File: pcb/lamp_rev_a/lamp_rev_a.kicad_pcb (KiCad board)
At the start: 4 copper layers, 100 x 80 mm, 107 parts, among them J1 TYPE-C 3.1 MT 16P, J2 DC-005-5A-2.0, J3 DB128H-5.08-2P-BK-S, Q1 AO3400A, Q2 MMBT3904, Q3 MMBT3904, Q4 MMBT3904, Q5 MMBT3904, Q6 MMBT3904, Q7 MMBT3904, Q8 MMBT3904, Q9 MMBT3904, U1 ESP32-S3-WROOM-1-N8, U2 USBLC6-2SC6, U3 AMS1117-3.3, U4 ADS1115IDGSR, U5 CD74HC4051M, U6 TLV6001IDBVR, U7 TC4427ACOA

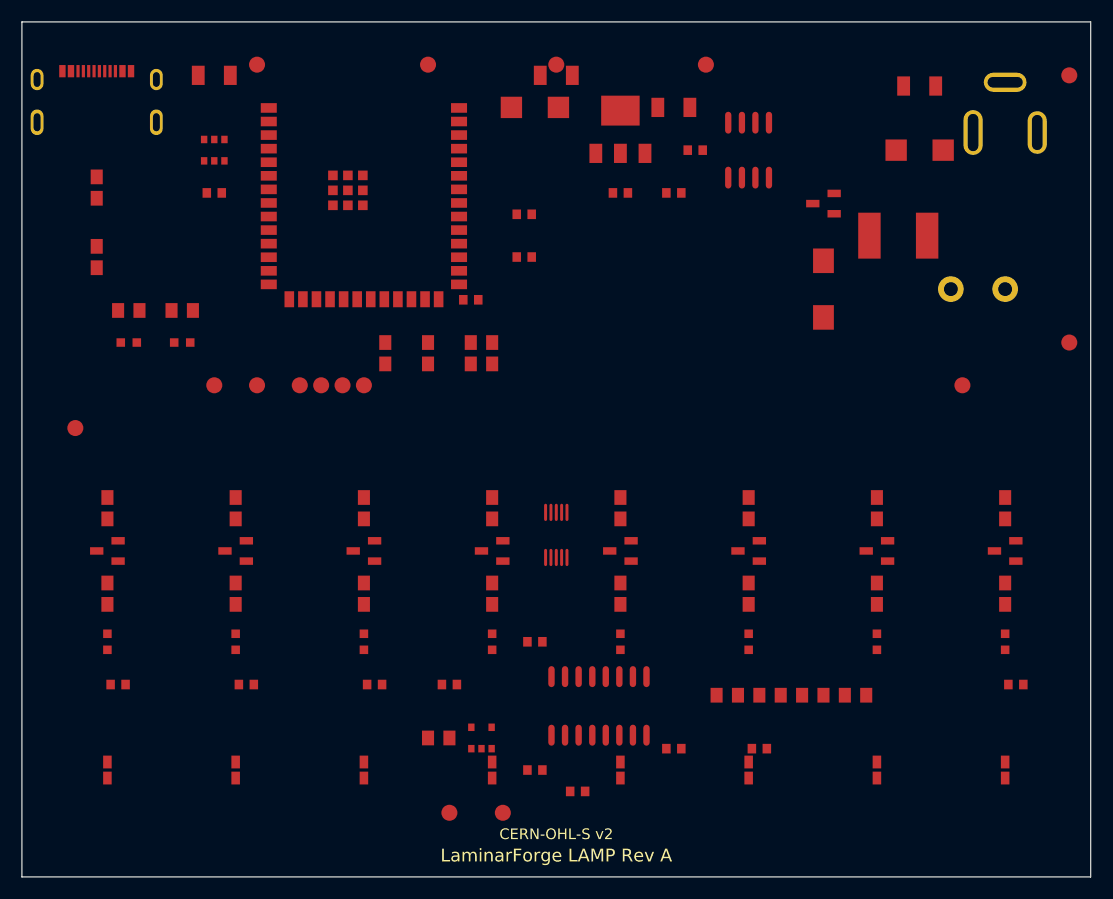
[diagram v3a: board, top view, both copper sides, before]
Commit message: Add LAMP Rev A routing seed workflow
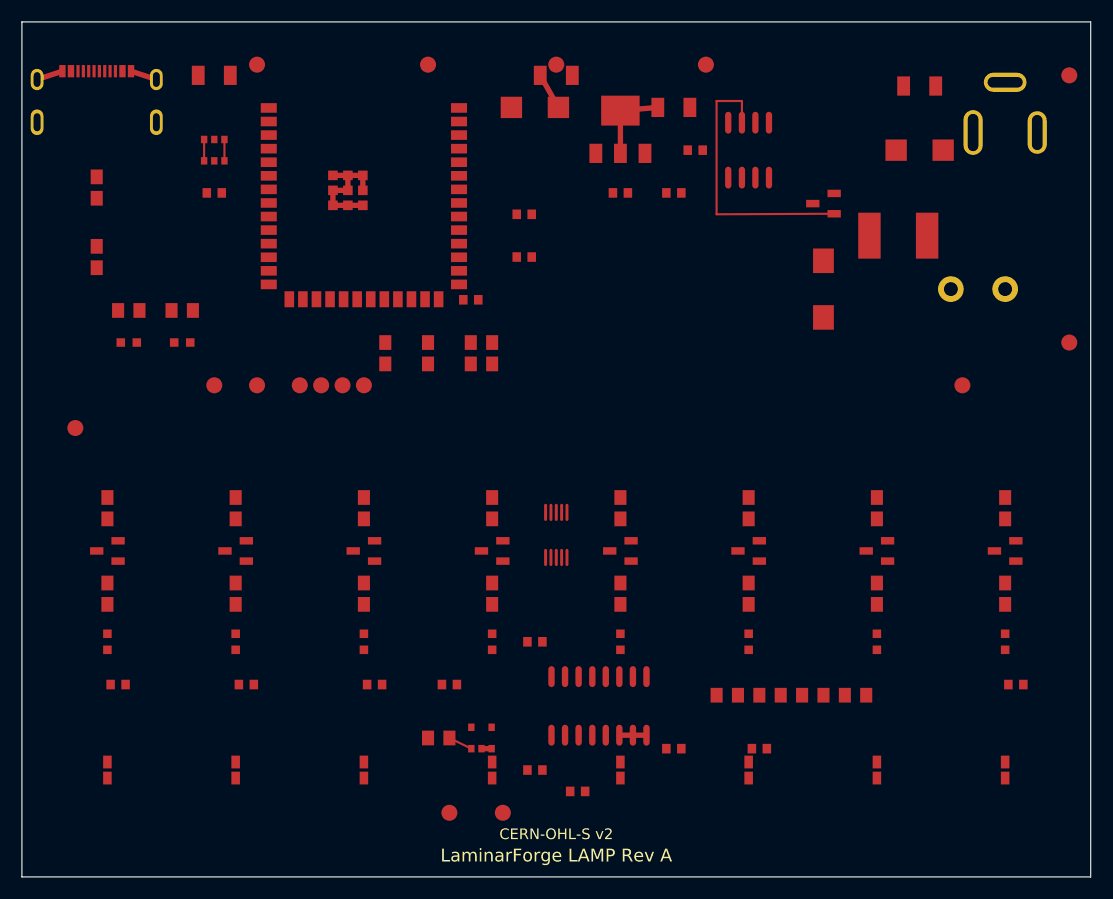
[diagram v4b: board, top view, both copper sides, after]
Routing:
- net GATE_DRV: track 0.00 -> 26.0 mm
- net GND: track 0.00 -> 19.7 mm
- net +3V3: track 0.00 -> 7.51 mm
- net +5V: track 0.00 -> 3.45 mm
- net ADC_AIN1: track 0.00 -> 2.28 mm
- net USB_DP: track 0.00 -> 2.00 mm
- net USB_DN: track 0.00 -> 2.00 mm
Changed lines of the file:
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@@
     (pad "1" smd circle (at 0 0) (size 1.5 1.5) (layers "F.Cu" "F.Mask") (net 22 "VBUS"))
   )
+  (segment
+    (start 3.790 4.610)
+    (end 1.420 5.390)
+    (width 0.500)
+    (layer "F.Cu")
+    (net 1)
+  )
+  (segment
+    (start 12.580 5.390)
+    (end 10.210 4.610)
+    (width 0.500)
+    (layer "F.Cu")
+    (net 1)
+  )
+  (segment
+    (start 29.100 17.160)
+    (end 29.100 15.760)
+    (width 0.500)
+    (layer "F.Cu")
+    (net 1)
+  )
+  (segment
+    (start 30.500 14.360)
+    (end 29.100 14.360)
+    (width 0.500)
+    (layer "F.Cu")
+    (net 1)
+  )
+  (segment
+    (start 30.500 15.760)
+    (end 29.100 15.760)
+    (width 0.500)
+    (layer "F.Cu")
+    (net 1)
+  )
+  (segment
+    (start 30.500 15.760)
+    (end 30.500 14.360)
+    (width 0.500)
+    (layer "F.Cu")
+    (net 1)
+  )
+  (segment
+    (start 30.500 17.160)
+    (end 29.100 17.160)
+    (width 0.500)
+    (layer "F.Cu")
+    (net 1)
+  )
+  (segment
+    (start 31.900 14.360)
+    (end 30.500 14.360)
+    (width 0.500)
+    (layer "F.Cu")
+    (net 1)
+  )
+  (segment
+    (start 31.900 15.760)
+    (end 31.900 14.360)
+    (width 0.500)
+    (layer "F.Cu")
+    (net 1)
+  )
+  (segment
+    (start 31.900 17.160)
+    (end 30.500 17.160)
+    (width 0.500)
+    (layer "F.Cu")
+    (net 1)
+  )
+  (segment
+    (start 43 68)
+    (end 43.950 68)
+    (width 0.500)
+    (layer "F.Cu")
+    (net 1)
+  )
+  (segment
+    (start 57.170 66.740)
+    (end 58.440 66.740)
+    (width 0.500)
+    (layer "F.Cu")
+    (net 1)
+  )
+  (segment
+    (start 57.170 66.740)
+    (end 55.900 66.740)
+    (width 0.500)
+    (layer "F.Cu")
+    (net 1)
+  )
+  (segment
+    (start 50.200 8)
+    (end 48.500 5)
+    (width 0.500)
+    (layer "F.Cu")
+    (net 4)
+  )
+  (segment
+    (start 56 12.300)
+    (end 56 8.300)
+    (width 0.500)
+    (layer "F.Cu")
+    (net 5)
+  )
+  (segment
+    (start 59.500 8)
+    (end 56 8.300)
+    (width 0.500)
+    (layer "F.Cu")
+    (net 5)
+  )
+  (segment
+    (start 42.050 68)
+    (end 40 67)
+    (width 0.200)
+    (layer "F.Cu")
+    (net 13)
+  )
+  (segment
+    (start 17.050 13)
+    (end 17.050 11)
+    (width 0.200)
+    (layer "F.Cu")
+    (net 18)
+  )
+  (segment
+    (start 18.950 13)
+    (end 18.950 11)
+    (width 0.200)
+    (layer "F.Cu")
+    (net 19)
+  )
+  (segment
+    (start 67.370 9.430)
+    (end 67.370 7.400)
+    (width 0.200)
+    (layer "F.Cu")
+    (net 10)
+  )
+  (segment
+    (start 67.370 7.400)
+    (end 65 7.400)
+    (width 0.200)
+    (layer "F.Cu")
+    (net 10)
+  )
+  (segment
+    (start 65 7.400)
+    (end 65 18)
+    (width 0.200)
+    (layer "F.Cu")
+    (net 10)
+  )
+  (segment
+    (start 65 18)
+    (end 76 17.950)
+    (width 0.200)
+    (layer "F.Cu")
+    (net 10)
+  )
 )

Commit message: Add LAMP Rev A copper zones
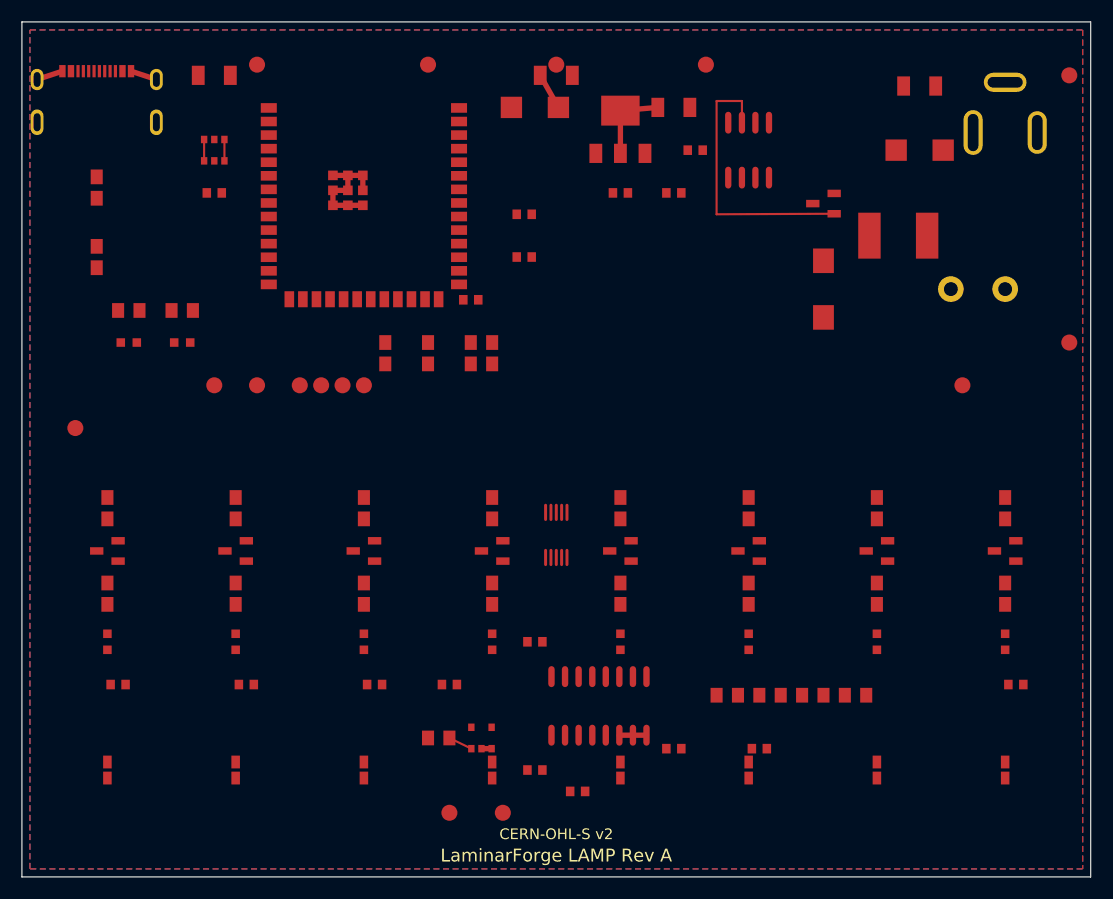
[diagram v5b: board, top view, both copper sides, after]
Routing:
- added copper zone on B.Cu, net GND
- added copper zone on F.Cu, net GND
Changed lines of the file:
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@@
     (net 10)
   )
+  (zone
+    (net 1)
+    (net_name "GND")
+    (layer "F.Cu")
+    (hatch edge 0.5)
+    (connect_pads yes (clearance 0.200))
+    (min_thickness 0.150)
+    (fill yes (thermal_gap 0.300) (thermal_bridge_width 0.300))
+    (polygon
+      (pts
+        (xy 0.750 0.750)
+        (xy 99.250 0.750)
+        (xy 99.250 79.250)
+        (xy 0.750 79.250)
+      )
+    )
+  )
+  (zone
+    (net 1)
+    (net_name "GND")
+    (layer "B.Cu")
+    (hatch edge 0.5)
+    (connect_pads yes (clearance 0.200))
+    (min_thickness 0.150)
+    (fill yes (thermal_gap 0.300) (thermal_bridge_width 0.300))
+    (polygon
+      (pts
+        (xy 0.750 0.750)
+        (xy 99.250 0.750)
+        (xy 99.250 79.250)
+        (xy 0.750 79.250)
+      )
+    )
+  )
 )

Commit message: Add LAMP Rev A greedy routing workflow
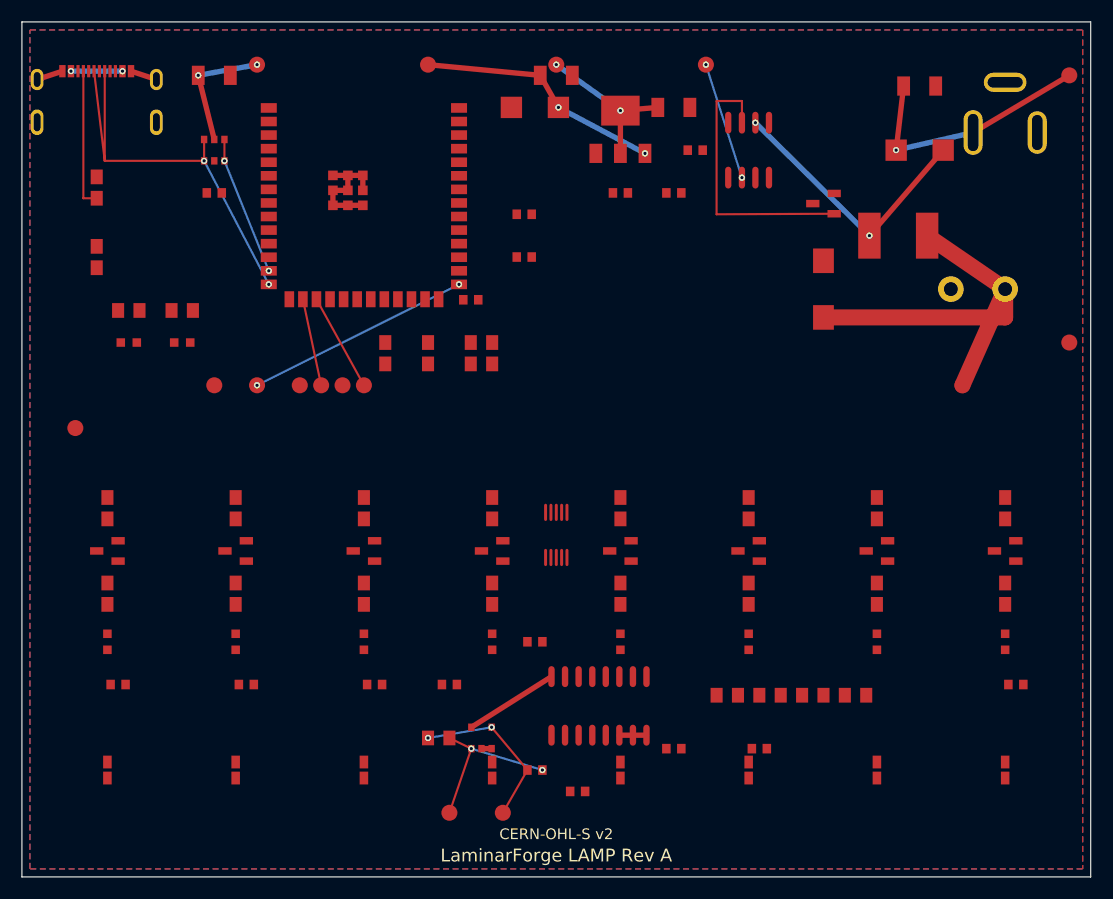
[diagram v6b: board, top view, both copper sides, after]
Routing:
- net USB_DP: track 2.00 -> 41.2 mm, vias 0 -> 2
- net HEATER_SUPPLY: track 0.00 -> 38.3 mm
- net +12V: track 0.00 -> 25.6 mm, vias 0 -> 2
- net +12V_RAW: track 0.00 -> 23.9 mm, vias 0 -> 2
- net ESP_GPIO0: track 0.00 -> 21.1 mm, vias 0 -> 2
- net +5V: track 3.45 -> 23.2 mm, vias 0 -> 2
- net VBUS: track 0.00 -> 16.6 mm, vias 0 -> 4
- net +3V3: track 7.51 -> 23.8 mm, vias 0 -> 2
- net MUX_COM: track 0.00 -> 15.9 mm, vias 0 -> 2
- net ADC_AIN1: track 2.28 -> 15.6 mm, vias 0 -> 2
- net USB_CC1: track 0.00 -> 13.1 mm
- net USB_DN: track 2.00 -> 13.1 mm, vias 0 -> 2
- net HEATER_PWM: track 0.00 -> 11.1 mm, vias 0 -> 2
- net SCL: track 0.00 -> 9.19 mm
- net SDA: track 0.00 -> 8.23 mm

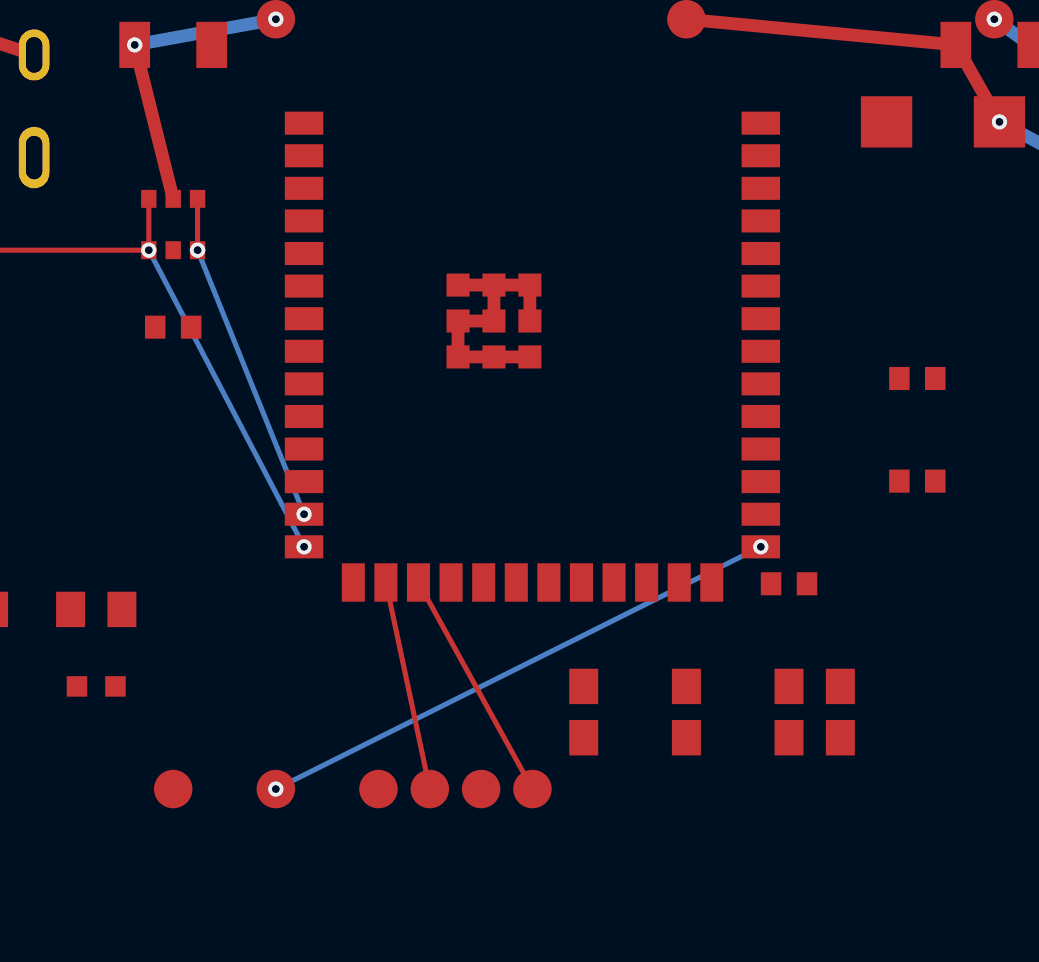
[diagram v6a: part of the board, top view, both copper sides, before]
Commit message: Move LAMP Rev A debug test points near ESP32
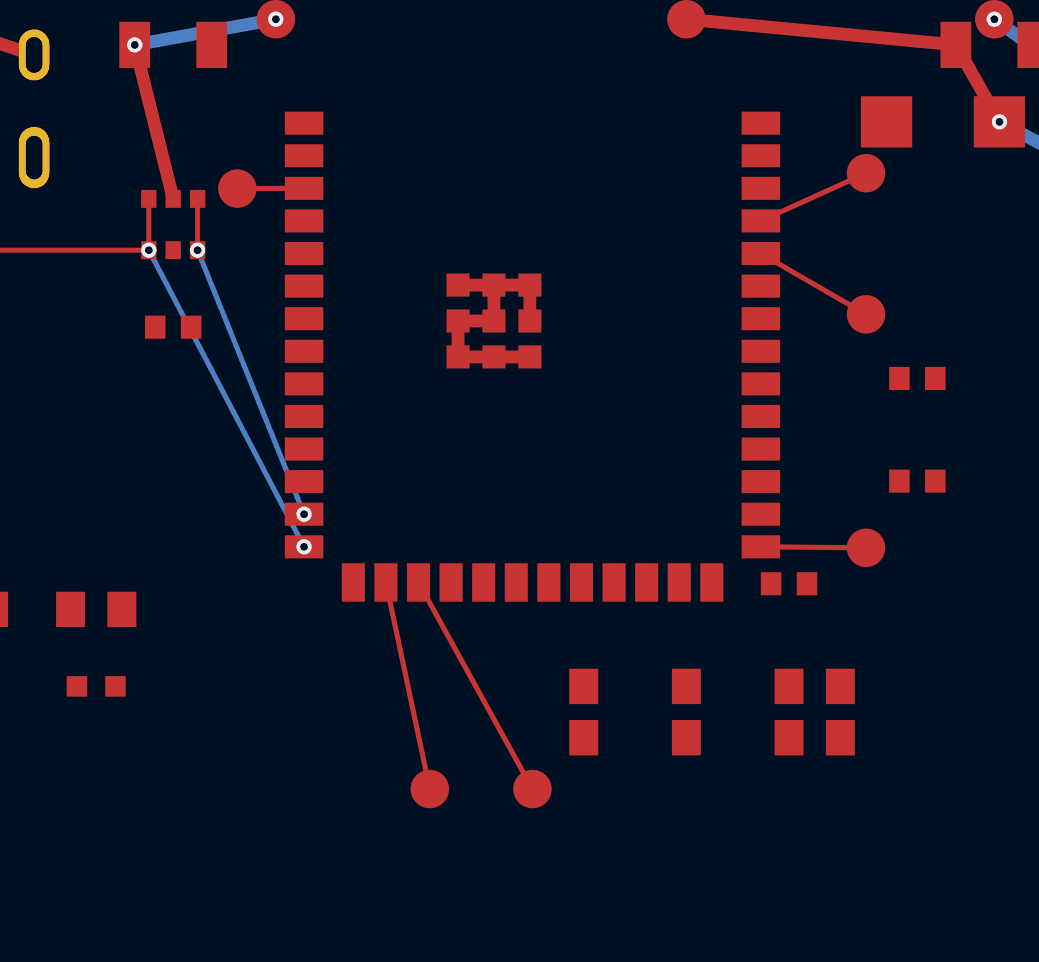
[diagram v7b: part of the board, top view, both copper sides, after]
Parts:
- moved TP_TX 30.6 mm to (45.0, 10.0)
- moved TP_BOOT 24.8 mm to (45.0, 24.6)
- moved TP_RX 23.8 mm to (45.0, 15.5)
- moved TP_EN 23.5 mm to (20.5, 10.6)
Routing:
- net ESP_GPIO0: track 21.1 -> 4.10 mm, vias 2 -> 0
- net UART_RX: track 0.00 -> 4.74 mm
- net UART_TX: track 0.00 -> 4.50 mm
- net ESP_EN: track 0.00 -> 2.60 mm
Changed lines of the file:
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@@
   (footprint "lcsc:TESTPOINT_SMD_1.5MM"
     (layer "F.Cu")
-    (at 18 34 0)
+    (at 20.500 10.600 0)
     (property "Reference" "TP_EN" (at 0 -1.8 0) (layer "F.Fab") (effects (font (size 0.8 0.8) (thickness 0.1))))
     (property "Value" "ESP_EN" (at 0 1.8 0) (layer "F.Fab") (effects (font (size 0.8 0.8) (thickness 0.1))))
@@
   (footprint "lcsc:TESTPOINT_SMD_1.5MM"
     (layer "F.Cu")
-    (at 22 34 0)
+    (at 45 24.600 0)
     (property "Reference" "TP_BOOT" (at 0 -1.8 0) (layer "F.Fab") (effects (font (size 0.8 0.8) (thickness 0.1))))
     (property "Value" "ESP_GPIO0" (at 0 1.8 0) (layer "F.Fab") (effects (font (size 0.8 0.8) (thickness 0.1))))
@@
   (footprint "lcsc:TESTPOINT_SMD_1.5MM"
     (layer "F.Cu")
-    (at 26 34 0)
+    (at 45 10 0)
     (property "Reference" "TP_TX" (at 0 -1.8 0) (layer "F.Fab") (effects (font (size 0.8 0.8) (thickness 0.1))))
     (property "Value" "UART_TX" (at 0 1.8 0) (layer "F.Fab") (effects (font (size 0.8 0.8) (thickness 0.1))))
@@
   (footprint "lcsc:TESTPOINT_SMD_1.5MM"
     (layer "F.Cu")
-    (at 30 34 0)
+    (at 45 15.500 0)
     (property "Reference" "TP_RX" (at 0 -1.8 0) (layer "F.Fab") (effects (font (size 0.8 0.8) (thickness 0.1))))
     (property "Value" "UART_RX" (at 0 1.8 0) (layer "F.Fab") (effects (font (size 0.8 0.8) (thickness 0.1))))
@@
     (net 7)
   )
-  (via
-    (at 22 34)
-    (size 0.6)
-    (drill 0.3)
-    (layers "F.Cu" "B.Cu")
+  (segment
+    (start 20.500 10.600)
+    (end 23.100 10.590)
+    (width 0.200)
+    (layer "F.Cu")
+    (net 23)
+  )
+  (segment
+    (start 40.900 24.560)
+    (end 45 24.600)
+    (width 0.200)
+    (layer "F.Cu")
     (net 24)
   )
-  (via
-    (at 40.900 24.560)
-    (size 0.6)
-    (drill 0.3)
-    (layers "F.Cu" "B.Cu")
-    (net 24)
-  )
-  (segment
-    (start 22 34)
-    (end 40.900 24.560)
-    (width 0.200)
-    (layer "B.Cu")
-    (net 24)
+  (segment
+    (start 40.900 11.860)
+    (end 45 10)
+    (width 0.200)
+    (layer "F.Cu")
+    (net 25)
+  )
+  (segment
+    (start 40.900 13.130)
+    (end 45 15.500)
+    (width 0.200)
+    (layer "F.Cu")
+    (net 26)
   )
   (zone

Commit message: Tighten LAMP Rev A routing workflow
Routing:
- net SCL: track 9.19 -> 29.9 mm
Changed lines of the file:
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@@
     (net 26)
+  )
+  (segment
+    (start 32 34)
+    (end 49 45.890)
+    (width 0.200)
+    (layer "F.Cu")
+    (net 12)
   )
   (zone
